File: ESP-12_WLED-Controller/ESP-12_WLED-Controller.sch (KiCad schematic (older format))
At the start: 21 parts, among them J1 Conn_01x02_Male, J2 Conn_01x04_Male, J3 Conn_01x03_Male, Q1 2N7000, SW1 SW_RST, U1 TS1117-3.3, U2 ESP-12E, U3 SN74LVC1T45DBV

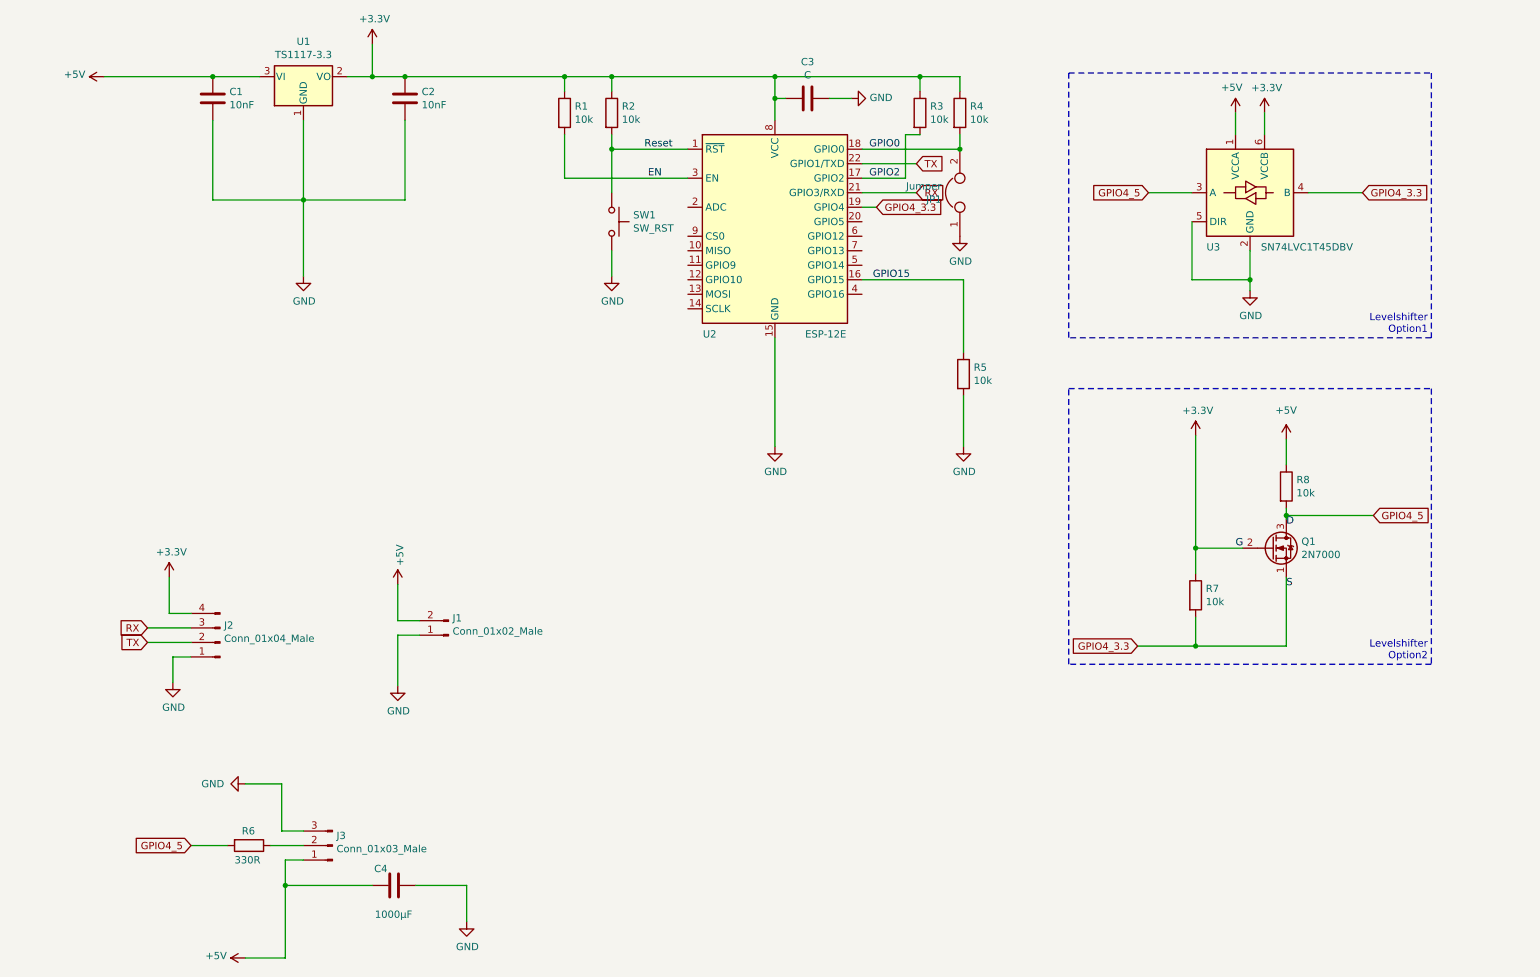
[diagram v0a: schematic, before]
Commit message: add IRF7410 Power MOSFET
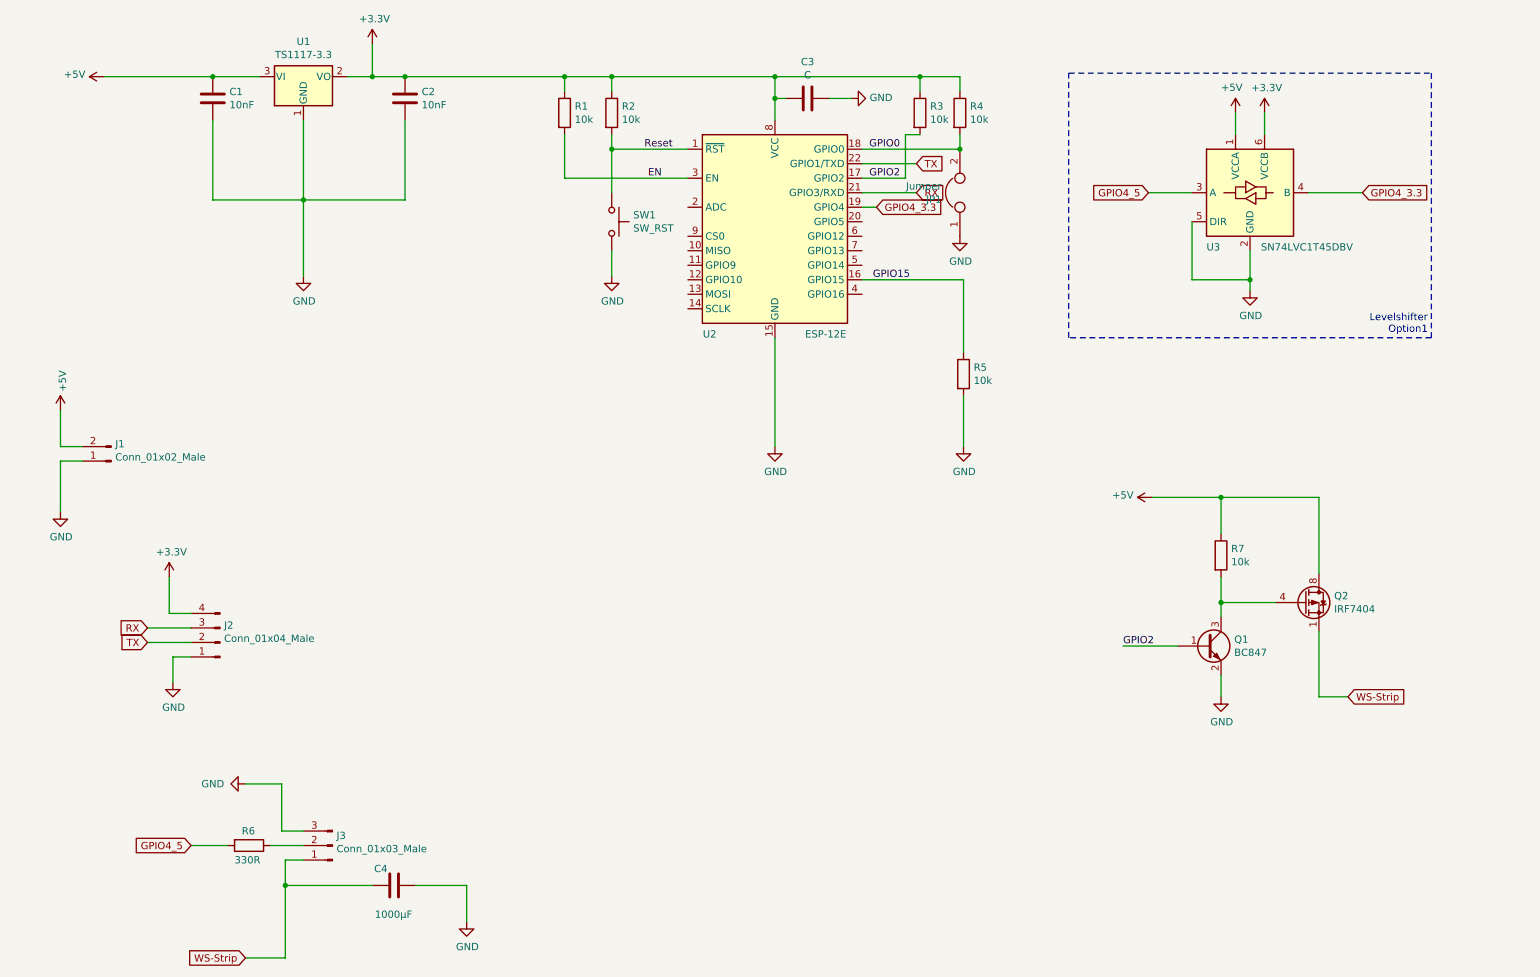
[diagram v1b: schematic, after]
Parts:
- removed Q1: 2N7000, Package_TO_SOT_SMD:SOT-23, symbol Transistor_FET:2N7000
- removed R8: 10k, Resistor_SMD:R_0805_2012Metric_Pad1.15x1.40mm_HandSolder, symbol Device:R
- added Q1: BC847, Package_TO_SOT_SMD:SOT-23, symbol Transistor_BJT:BC847
- added Q2: IRF7404, Package_SO:SOIC-8_3.9x4.9mm_P1.27mm, symbol Transistor_FET:IRF7404
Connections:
- net +3V3: no longer R7.1
- net +5V: now also R7.1, Q2.5 (D), Q2.6 (D), Q2.7 (D), Q2.8 (D); no longer C4.1, J3.1 (Pin_1)
- net GND: now also Q1.2 (E)
- net GPIO2: now also Q1.1 (B)
- net GPIO4_3.3: no longer R7.2
- new net: Q1.3 (C), Q2.4 (G), R7.2
- new net WS-Strip: C4.1, J3.1 (Pin_1), Q2.1 (S), Q2.2 (S), Q2.3 (S)
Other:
- note removed: "Levelshifter\nOption2\n"
- moved on the sheet: J1
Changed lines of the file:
@@
 	9175 2600 9175 2400
-$Comp
-L power:+5V #PWR013
-U 1 1 60CC786A
-P 2250 7275
-F 0 "#PWR013" H 2250 7125 50  0001 C CNN
-F 1 "+5V" V 2265 7403 50  0000 L CNN
-F 2 "" H 2250 7275 50  0001 C CNN
-F 3 "" H 2250 7275 50  0001 C CNN
-	1    2250 7275
-	0    -1   -1   0
-$EndComp
 $Comp
 L power:GND #PWR014
@@
 L Connector:Conn_01x02_Male J1
 U 1 1 60CD0E2A
-P 3650 5050
-F 0 "J1" H 3622 4932 50  0000 R CNN
-F 1 "Conn_01x02_Male" H 3622 5023 50  0000 R CNN
-F 2 "TerminalBlock_Phoenix:TerminalBlock_Phoenix_MKDS-1,5-2_1x02_P5.00mm_Horizontal" H 3650 5050 50  0001 C CNN
-F 3 "~" H 3650 5050 50  0001 C CNN
-	1    3650 5050
+P 1325 3850
+F 0 "J1" H 1297 3732 50  0000 R CNN
+F 1 "Conn_01x02_Male" H 1297 3823 50  0000 R CNN
+F 2 "TerminalBlock_Phoenix:TerminalBlock_Phoenix_MKDS-1,5-2_1x02_P5.00mm_Horizontal" H 1325 3850 50  0001 C CNN
+F 3 "~" H 1325 3850 50  0001 C CNN
+	1    1325 3850
 	-1   0    0    1
 $EndComp
@@
 L power:+5V #PWR03
 U 1 1 60CD1AA8
-P 3300 4700
-F 0 "#PWR03" H 3300 4550 50  0001 C CNN
-F 1 "+5V" V 3315 4828 50  0000 L CNN
-F 2 "" H 3300 4700 50  0001 C CNN
-F 3 "" H 3300 4700 50  0001 C CNN
-	1    3300 4700
-	1    0    0    -1
-$EndComp
-Wire Wire Line
-	3300 4700 3300 4950
-Wire Wire Line
-	3300 4950 3450 4950
+P 975 3500
+F 0 "#PWR03" H 975 3350 50  0001 C CNN
+F 1 "+5V" V 990 3628 50  0000 L CNN
+F 2 "" H 975 3500 50  0001 C CNN
+F 3 "" H 975 3500 50  0001 C CNN
+	1    975  3500
+	1    0    0    -1
+$EndComp
+Wire Wire Line
+	975  3500 975  3750
+Wire Wire Line
+	975  3750 1125 3750
 $Comp
 L power:GND #PWR04
 U 1 1 60CD3285
-P 3300 5400
-F 0 "#PWR04" H 3300 5150 50  0001 C CNN
-F 1 "GND" H 3305 5227 50  0000 C CNN
-F 2 "" H 3300 5400 50  0001 C CNN
-F 3 "" H 3300 5400 50  0001 C CNN
-	1    3300 5400
-	1    0    0    -1
-$EndComp
-Wire Wire Line
-	3300 5400 3300 5050
-Wire Wire Line
-	3300 5050 3450 5050
+P 975 4200
+F 0 "#PWR04" H 975 3950 50  0001 C CNN
+F 1 "GND" H 980 4027 50  0000 C CNN
+F 2 "" H 975 4200 50  0001 C CNN
+F 3 "" H 975 4200 50  0001 C CNN
+	1    975  4200
+	1    0    0    -1
+$EndComp
+Wire Wire Line
+	975  4200 975  3850
+Wire Wire Line
+	975  3850 1125 3850
 $Comp
 L Connector:Conn_01x04_Male J2
@@
 	2425 6500 2650 6500
 Connection ~ 7175 1700
-$Comp
-L Transistor_FET:2N7000 Q1
-U 1 1 60CC61B7
-P 9325 4450
-F 0 "Q1" H 9529 4496 50  0000 L CNN
-F 1 "2N7000" H 9529 4405 50  0000 L CNN
-F 2 "Package_TO_SOT_SMD:SOT-23" H 9525 4375 50  0001 L CIN
-F 3 "https://www.fairchildsemi.com/datasheets/2N/2N7000.pdf" H 9325 4450 50  0001 L CNN
-	1    9325 4450
-	1    0    0    -1
-$EndComp
-$Comp
-L Device:R R7
-U 1 1 60CC8C8B
-P 8800 4775
-F 0 "R7" H 8870 4821 50  0000 L CNN
-F 1 "10k" H 8870 4730 50  0000 L CNN
-F 2 "Resistor_SMD:R_0805_2012Metric_Pad1.15x1.40mm_HandSolder" V 8730 4775 50  0001 C CNN
-F 3 "~" H 8800 4775 50  0001 C CNN
-	1    8800 4775
-	1    0    0    -1
-$EndComp
-Text GLabel 8400 5125 0    50   Input ~ 0
-GPIO4_3.3
-$Comp
-L power:+3.3V #PWR0101
-U 1 1 60CC977C
-P 8800 3675
-F 0 "#PWR0101" H 8800 3525 50  0001 C CNN
-F 1 "+3.3V" H 8815 3848 50  0000 C CNN
-F 2 "" H 8800 3675 50  0001 C CNN
-F 3 "" H 8800 3675 50  0001 C CNN
-	1    8800 3675
-	1    0    0    -1
-$EndComp
-$Comp
-L Device:R R8
-U 1 1 60CCB244
-P 9425 4025
-F 0 "R8" H 9495 4071 50  0000 L CNN
-F 1 "10k" H 9495 3980 50  0000 L CNN
-F 2 "Resistor_SMD:R_0805_2012Metric_Pad1.15x1.40mm_HandSolder" V 9355 4025 50  0001 C CNN
-F 3 "~" H 9425 4025 50  0001 C CNN
-	1    9425 4025
-	1    0    0    -1
-$EndComp
-$Comp
-L power:+5V #PWR0103
-U 1 1 60CD032E
-P 9425 3700
-F 0 "#PWR0103" H 9425 3550 50  0001 C CNN
-F 1 "+5V" H 9350 3900 50  0000 L CNN
-F 2 "" H 9425 3700 50  0001 C CNN
-F 3 "" H 9425 3700 50  0001 C CNN
-	1    9425 3700
-	1    0    0    -1
-$EndComp
-Wire Wire Line
-	9125 4450 8800 4450
-Wire Wire Line
-	8800 4450 8800 3675
-Wire Wire Line
-	8800 4450 8800 4625
-Connection ~ 8800 4450
-Wire Wire Line
-	8400 5125 8800 5125
-Wire Wire Line
-	8800 5125 8800 4925
-Wire Wire Line
-	8800 5125 9425 5125
-Wire Wire Line
-	9425 5125 9425 4650
-Connection ~ 8800 5125
-Wire Wire Line
-	9425 3700 9425 3875
-Text GLabel 10025 4225 2    50   Input ~ 0
-GPIO4_5
 Wire Notes Line
 	7925 1175 10425 1175
@@
 Wire Notes Line
 	7925 3000 7925 1175
-Wire Notes Line
-	7925 3350 10425 3350
-Wire Notes Line
-	10425 3350 10425 5250
-Wire Notes Line
-	10425 5250 7925 5250
-Wire Notes Line
-	7925 5250 7925 3350
-Wire Wire Line
-	9425 4175 9425 4225
-Wire Wire Line
-	9425 4225 10025 4225
-Connection ~ 9425 4225
-Wire Wire Line
-	9425 4225 9425 4250
 Text Notes 10400 2975 2    50   ~ 0
 Levelshifter\nOption1
-Text Notes 10400 5225 2    50   ~ 0
-Levelshifter\nOption2\n
-Text Label 9425 4725 0    50   ~ 0
-S
-Text Label 9075 4450 0    50   ~ 0
-G
-Text Label 9425 4300 0    50   ~ 0
-D
 Wire Wire Line
 	1275 1200 2025 1200
@@
 	1    0    0    -1
 $EndComp
+$Comp
+L Transistor_BJT:BC847 Q1
+U 1 1 60D13373
+P 8875 5125
+F 0 "Q1" H 9066 5171 50  0000 L CNN
+F 1 "BC847" H 9066 5080 50  0000 L CNN
+F 2 "Package_TO_SOT_SMD:SOT-23" H 9075 5050 50  0001 L CIN
+F 3 "http://www.infineon.com/dgdl/Infineon-BC847SERIES_BC848SERIES_BC849SERIES_BC850SERIES-DS-v01_01-en.pdf?fileId=db3a304314dca389011541d4630a1657" H 8875 5125 50  0001 L CNN
+	1    8875 5125
+	1    0    0    -1
+$EndComp
+$Comp
+L Device:R R7
+U 1 1 60D14566
+P 8975 4500
+F 0 "R7" H 9045 4546 50  0000 L CNN
+F 1 "10k" H 9045 4455 50  0000 L CNN
+F 2 "Resistor_SMD:R_0805_2012Metric_Pad1.15x1.40mm_HandSolder" V 8905 4500 50  0001 C CNN
+F 3 "~" H 8975 4500 50  0001 C CNN
+	1    8975 4500
+	1    0    0    -1
+$EndComp
+$Comp
+L power:GND #PWR0101
+U 1 1 60D151C8
+P 8975 5475
+F 0 "#PWR0101" H 8975 5225 50  0001 C CNN
+F 1 "GND" H 8980 5302 50  0000 C CNN
+F 2 "" H 8975 5475 50  0001 C CNN
+F 3 "" H 8975 5475 50  0001 C CNN
+	1    8975 5475
+	1    0    0    -1
+$EndComp
+Wire Wire Line
+	8975 4825 9350 4825
+Connection ~ 8975 4825
+Wire Wire Line
+	8975 5475 8975 5325
+$Comp
+L power:+5V #PWR0103
+U 1 1 60D1C6F6
+P 8500 4100
+F 0 "#PWR0103" H 8500 3950 50  0001 C CNN
+F 1 "+5V" V 8515 4228 50  0000 L CNN
+F 2 "" H 8500 4100 50  0001 C CNN
+F 3 "" H 8500 4100 50  0001 C CNN
+	1    8500 4100
+	0    -1   -1   0
+$EndComp
+Wire Wire Line
+	8500 4100 8975 4100
+Wire Wire Line
+	8975 4350 8975 4100
+Connection ~ 8975 4100
+Wire Wire Line
+	8975 4100 9650 4100
+Wire Wire Line
+	8975 4825 8975 4925
+Wire Wire Line
+	8975 4650 8975 4825
+Wire Wire Line
+	9650 5025 9650 5475
+$Comp
+L Transistor_FET:IRF7404 Q2
+U 1 1 60D66B04
+P 9550 4825
+F 0 "Q2" H 9755 4871 50  0000 L CNN
+F 1 "IRF7404" H 9755 4780 50  0000 L CNN
+F 2 "Package_SO:SOIC-8_3.9x4.9mm_P1.27mm" H 9750 4750 50  0001 L CIN
+F 3 "http://www.infineon.com/dgdl/irf7404.pdf?fileId=5546d462533600a4015355fa2b5b1b9e" V 9550 4825 50  0001 L CNN
+	1    9550 4825
+	1    0    0    -1
+$EndComp
+Wire Wire Line
+	9650 4100 9650 4625
+Text GLabel 9850 5475 2    50   Input ~ 0
+WS-Strip
+Wire Wire Line
+	9850 5475 9650 5475
+Text GLabel 2250 7275 0    50   Input ~ 0
+WS-Strip
+Text Label 8300 5125 0    50   ~ 0
+GPIO2
+Wire Wire Line
+	8300 5125 8675 5125
 $EndSCHEMATC

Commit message: LLC changes
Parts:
- removed Q1: BC847, Package_TO_SOT_SMD:SOT-23, symbol Transistor_BJT:BC847
- removed U3: SN74LVC1T45DBV, Package_TO_SOT_SMD:SOT-23-6, symbol Logic_LevelTranslator:SN74LVC1T45DBV
- added D1: SS14, Diode_SMD:D_SMA_Handsoldering, symbol Device:D
- added Q1: TSM2302CX, Package_TO_SOT_SMD:SOT-23, symbol Transistor_FET:TSM2302CX
- added R8: 10k, Resistor_SMD:R_0805_2012Metric_Pad1.15x1.40mm_HandSolder, symbol Device:R
- added U4: 74LVC1G125, Package_SO:TSOP-5_1.65x3.05mm_P0.95mm, symbol 74xGxx:74LVC1G125
- added altQ2: alt. MOSFET, Package_TO_SOT_THT:TO-220-3_Vertical, symbol Transistor_FET:IRF9540N
- Q2: value IRF7404 -> IRF7410
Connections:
- net +5V: now also Q2.1 (S), Q2.2 (S), Q2.3 (S), U4.5 (VCC), altQ2.3 (S); no longer Q2.5 (D), Q2.6 (D), Q2.7 (D), Q2.8 (D)
- net GND: now also D1.2 (A), Q1.2 (S), R8.2, U4.1, U4.3 (GND)
- net GPIO4_3.3: now also U4.2
- net GPIO4_5: now also U4.4
- net RELAY: now reaches U2.6 (GPIO12)
- net RELAY: now also Q1.1 (G), R8.1
- net at Q2.4 (G), R7.2: now also Q1.3 (D), altQ2.1 (G)
- removed net WS-Strip: C4.1, J3.1 (Pin_1), Q2.1 (S), Q2.2 (S), Q2.3 (S)
- new net WS-Strip_VCC: C4.1, D1.1 (K), J3.1 (Pin_1), Q2.5 (D), Q2.6 (D), Q2.7 (D), Q2.8 (D), altQ2.2 (D)
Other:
- note removed: "Levelshifter\nOption1"
- moved on the sheet: C1, C2, C3, C4, J1, J2, J3, JP1, Q2, R1, R2, R3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
